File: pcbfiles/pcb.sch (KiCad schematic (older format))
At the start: 236 parts, among them J1 Conn_01x04_Female, J10 Conn_01x05, J2 Conn_01x05, J3 Conn_01x05, J4 Conn_01x05, J5 Conn_01x05, J6 Conn_01x04_Female, J7 Conn_01x05, J8 Conn_01x05, J9 Conn_01x05, Q1 AO3401A, Q2 AO3401A, SW1 SW_SPST, SW10 SW_SPST, SW11 SW_SPST, SW12 SW_SPST, SW13 SW_SPST, SW14 SW_SPST, SW15 SW_SPST, SW16 SW_SPST, SW17 SW_SPST, SW18 SW_SPST, SW19 SW_SPST, SW2 SW_SPST, SW20 SW_SPST, SW21 SW_SPST, SW22 SW_SPST, SW23 SW_SPST, SW24 SW_SPST, SW25 SW_SPST, SW26 SW_SPST, SW27 SW_SPST, SW28 SW_SPST, SW29 SW_SPST, SW3 SW_SPST, SW30 SW_SPST, SW31 SW_SPST, SW32 SW_SPST, SW33 SW_SPST, SW34 SW_SPST, SW35 SW_SPST, SW36 SW_SPST, SW37 SW_SPST, SW38 SW_SPDT, SW39 SW_SPST, SW4 SW_SPST, SW40 SW_SPST, SW41 SW_SPST, SW42 SW_SPST, SW43 SW_SPST, SW44 SW_SPST, SW45 SW_SPST, SW46 Rotary_Encoder_Switch, SW47 SW_SPDT, SW48 SW_SPST, SW49 SW_SPST, SW5 SW_SPST, SW50 SW_SPST, SW51 SW_SPST, SW52 SW_SPST, SW53 SW_SPST, SW54 SW_SPST, SW55 SW_SPST, SW56 SW_SPST, SW57 SW_SPST, SW58 SW_SPST, SW59 SW_SPST, SW6 SW_SPST, SW60 SW_SPST, SW61 SW_SPST, SW62 SW_SPST, SW63 SW_SPST, SW64 SW_SPST, SW65 SW_SPST, SW66 SW_SPST, SW67 SW_SPST, SW68 SW_SPST, SW69 SW_SPST, SW7 SW_SPST, SW70 SW_SPST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

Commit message: Final commit for the day.
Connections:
- net DB2_ROW_B is gone; now on net DB2_ROW0_B: J9.4 (Pin_4)
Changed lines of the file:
@@
 DB2_COL2_B
 Text GLabel 25750 6700 3    50   Input ~ 0
-DB2_ROW_B
+DB2_ROW0_B
 $Comp
 L power:GND1 #PWR0133

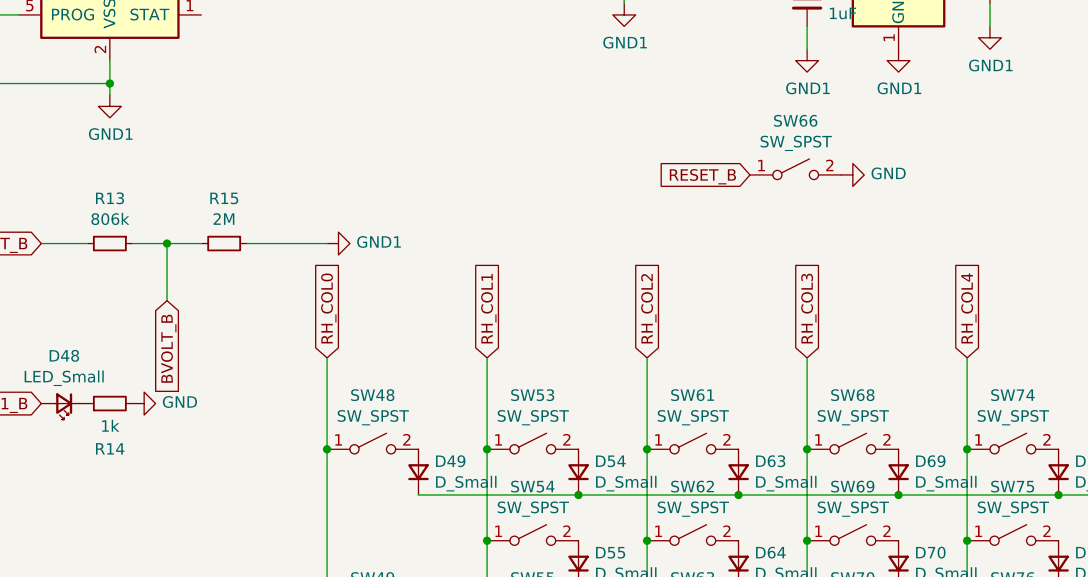
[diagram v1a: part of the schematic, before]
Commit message: Step file, various kinds of progress.
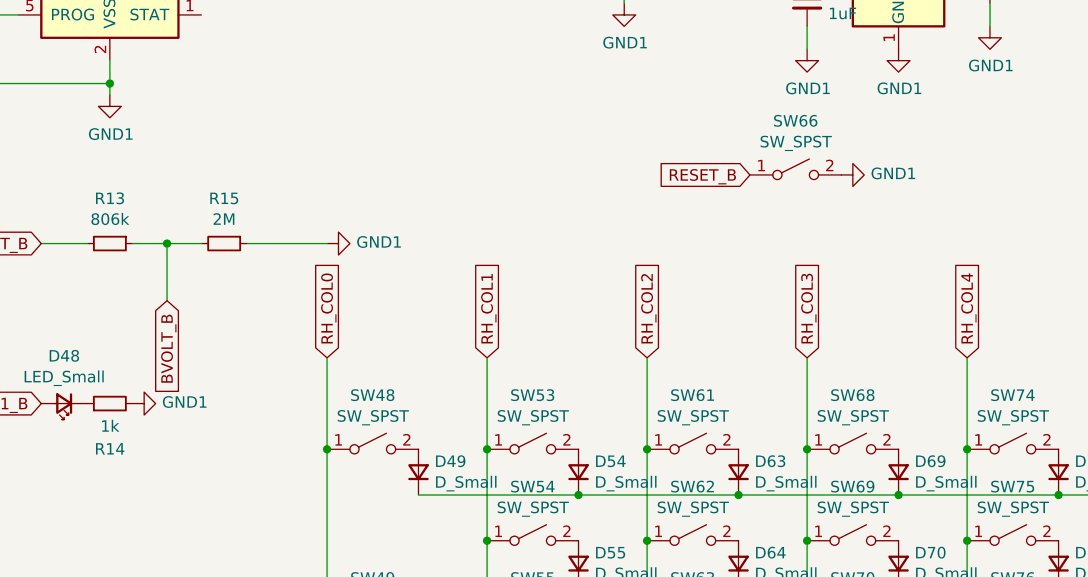
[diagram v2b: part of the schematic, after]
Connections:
- net GND: no longer R14.2, SW66.2 (B)
- net GND1: now also R14.2, SW66.2 (B)
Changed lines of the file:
@@
 $EndComp
 $Comp
-L power:GND #PWR0117
+L power:GND1 #PWR0117
 U 1 1 6132A644
 P 23450 2500
 F 0 "#PWR0117" H 23450 2250 50  0001 C CNN
-F 1 "GND" V 23455 2372 50  0000 R CNN
+F 1 "GND1" V 23455 2372 50  0000 R CNN
 F 2 "" H 23450 2500 50  0001 C CNN
 F 3 "" H 23450 2500 50  0001 C CNN
@@
 $EndComp
 $Comp
-L power:GND #PWR0118
+L power:GND1 #PWR0118
 U 1 1 6132A659
 P 20350 3500
 F 0 "#PWR0118" H 20350 3250 50  0001 C CNN
-F 1 "GND" V 20355 3372 50  0000 R CNN
+F 1 "GND1" V 20355 3372 50  0000 R CNN
 F 2 "" H 20350 3500 50  0001 C CNN
 F 3 "" H 20350 3500 50  0001 C CNN

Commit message: Routing progress.
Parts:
- BT1, BT3: footprint custom-parts:JST_PH_S2B-PH-K_1x02_P2.00mm_Horizontal -> Connector_JST:JST_PH_S2B-PH-K_1x02_P2.00mm_Horizontal
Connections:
- net DB1_COL0: now also U4.8 (P0.28)
- net DB1_COL1: now also U4.7 (P0.02)
- net DB1_ROW0: now also U4.6 (P0.03)
- net DB1_ROW1: now also U4.4 (P1.13)
- net LH_COL0: now also U4.2 (P1.11)
- net LH_COL1: now also U4.3 (P1.10)
- net LH_COL2: now also U4.10 (P0.30)
- net LH_ROW3: now also U4.9 (P0.29)
- net LH_ROW4: now also U4.11 (P0.31)
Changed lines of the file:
@@
 F 0 "BT1" V 4845 2100 50  0000 C CNN
 F 1 "Battery_Cell" V 4936 2100 50  0000 C CNN
-F 2 "custom-parts:JST_PH_S2B-PH-K_1x02_P2.00mm_Horizontal" V 5100 2110 50  0001 C CNN
+F 2 "Connector_JST:JST_PH_S2B-PH-K_1x02_P2.00mm_Horizontal" V 5100 2110 50  0001 C CNN
 F 3 "~" V 5100 2110 50  0001 C CNN
 	1    5100 2050
@@
 F 0 "BT3" V 19195 7050 50  0000 C CNN
 F 1 "Battery_Cell" V 19286 7050 50  0000 C CNN
-F 2 "custom-parts:JST_PH_S2B-PH-K_1x02_P2.00mm_Horizontal" V 19450 7060 50  0001 C CNN
+F 2 "Connector_JST:JST_PH_S2B-PH-K_1x02_P2.00mm_Horizontal" V 19450 7060 50  0001 C CNN
 F 3 "~" V 19450 7060 50  0001 C CNN
 	1    19450 7000
@@
 	21200 4900 21200 5700
 Connection ~ 21200 3700
+Text GLabel 900  4700 0    50   Input ~ 0
+LH_COL0
+Text GLabel 900  4800 0    50   Input ~ 0
+LH_COL1
+Text GLabel 900  5500 0    50   Input ~ 0
+LH_COL2
+Text GLabel 900  5300 0    50   Input ~ 0
+DB1_COL0
+Text GLabel 900  5200 0    50   Input ~ 0
+DB1_COL1
+Text GLabel 900  5100 0    50   Input ~ 0
+DB1_ROW0
+Text GLabel 900  4900 0    50   Input ~ 0
+DB1_ROW1
+Text GLabel 900  5400 0    50   Input ~ 0
+LH_ROW3
+Text GLabel 900  5600 0    50   Input ~ 0
+LH_ROW4
 $EndSCHEMATC

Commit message: more routing
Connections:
- net DB2_COL0_B: now also U1.11 (P0.31)
- net DB2_COL1_B: now also U1.10 (P0.30)
- net DB2_COL2_B: now also U1.9 (P0.29)
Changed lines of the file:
@@
 Text GLabel 900  5600 0    50   Input ~ 0
 LH_ROW4
+Text GLabel 16900 5600 0    50   Input ~ 0
+DB2_COL0_B
+Text GLabel 16900 5500 0    50   Input ~ 0
+DB2_COL1_B
+Text GLabel 16900 5400 0    50   Input ~ 0
+DB2_COL2_B
 $EndSCHEMATC

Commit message: Save most recent routing.
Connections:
- net DB1_COL0_B: now also U1.26 (P0.22)
- net DB1_COL1_B: now also U1.27 (P1.00)
- net DB1_ROW0_B: now also U1.28 (P1.03)
- net DB1_ROW1_B: now also U1.29 (P1.01)
- net DB2_ROW0_B: now also U1.8 (P0.28)
- net ENC_A_B: now also U1.2 (P1.11)
- net ENC_B_B: now also U1.3 (P1.10)
- net ENC_P1_B: now also U1.4 (P1.13)
- net RH_COL1: now also U1.18 (P0.23)
- net RH_COL2: now also U1.17 (P0.12)
- net RH_COL3: now also U1.16 (P1.09), U1.7 (P0.02)
- net RH_COL4: now also U1.15 (P0.07)
- net RH_COL5: now also U1.35 (P0.09)
- net RH_COL6: now also U1.36 (P0.10)
- net RH_ROW0: now also U1.33 (P1.04)
- net RH_ROW1: now also U1.34 (P1.06)
- net RH_ROW2: now also U1.30 (P1.02)
- net RH_ROW3: now also U1.20 (P0.19)
- net RH_ROW4: now also U1.13 (P0.05)
- net RH_ROW5: now also U1.6 (P0.03)
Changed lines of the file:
@@
 Text GLabel 16900 5400 0    50   Input ~ 0
 DB2_COL2_B
+Text GLabel 16900 5300 0    50   Input ~ 0
+DB2_ROW0_B
+Text GLabel 16900 5200 0    50   Input ~ 0
+RH_COL3
+Text GLabel 16900 5100 0    50   Input ~ 0
+RH_ROW5
+Text GLabel 16900 5800 0    50   Input ~ 0
+RH_ROW4
+Text GLabel 17500 6300 3    50   Input ~ 0
+RH_COL1
+Text GLabel 17200 6300 3    50   Input ~ 0
+RH_COL4
+Text GLabel 17300 6300 3    50   Input ~ 0
+RH_COL3
+Text GLabel 17400 6300 3    50   Input ~ 0
+RH_COL2
+Text GLabel 18300 5700 2    50   Input ~ 0
+DB1_COL0_B
+Text GLabel 18300 5600 2    50   Input ~ 0
+DB1_COL1_B
+Text GLabel 18300 5500 2    50   Input ~ 0
+DB1_ROW0_B
+Text GLabel 18300 5400 2    50   Input ~ 0
+DB1_ROW1_B
+Text GLabel 18300 4700 2    50   Input ~ 0
+RH_COL6
+Text GLabel 18300 4800 2    50   Input ~ 0
+RH_COL5
+Text GLabel 17700 6300 3    50   Input ~ 0
+RH_ROW3
+Text GLabel 18300 5300 2    50   Input ~ 0
+RH_ROW2
+Text GLabel 18300 4900 2    50   Input ~ 0
+RH_ROW1
+Text GLabel 18300 5000 2    50   Input ~ 0
+RH_ROW0
+Text GLabel 16900 4900 0    50   Input ~ 0
+RH_COL0
+Text GLabel 16900 4800 0    30   Input ~ 0
+ENC_B_B
+Text GLabel 16900 4700 0    30   Input ~ 0
+ENC_A_B
 $EndSCHEMATC

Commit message: Finish all basic routing!
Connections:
- net DB2_COL0: now also U4.19 (P0.21)
- net DB2_COL1: now also U4.18 (P0.23)
- net DB2_COL2: now also U4.17 (P0.12)
- net DB2_ROW0: now also U4.16 (P1.09)
- net ENC_A: now also U4.33 (P1.04)
- net ENC_B: now also U4.30 (P1.02)
- net ENC_P1: now also U4.34 (P1.06)
- net LH_COL3: now also U4.20 (P0.19)
- net LH_COL4: now also U4.26 (P0.22)
- net LH_COL5: now also U4.35 (P0.09)
- net LH_ROW0: now also U4.27 (P1.00)
- net LH_ROW1: now also U4.28 (P1.03)
- net LH_ROW2: now also U4.29 (P1.01)
- net LH_ROW5: now also U4.36 (P0.10)
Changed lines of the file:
@@
 Text GLabel 16900 4700 0    30   Input ~ 0
 ENC_A_B
+Text GLabel 1700 6300 3    50   Input ~ 0
+LH_COL3
+Text GLabel 2300 4800 2    50   Input ~ 0
+LH_COL5
+Text GLabel 1600 6300 3    50   Input ~ 0
+DB2_COL0
+Text GLabel 1500 6300 3    50   Input ~ 0
+DB2_COL1
+Text GLabel 1400 6300 3    50   Input ~ 0
+DB2_COL2
+Text GLabel 1300 6300 3    50   Input ~ 0
+DB2_ROW0
+Text GLabel 2300 4900 2    50   Input ~ 0
+LH_COL6
+Text GLabel 2300 4700 2    50   Input ~ 0
+LH_ROW5
+Text GLabel 2300 5700 2    50   Input ~ 0
+LH_COL4
+Text GLabel 2300 5000 2    30   Input ~ 0
+ENC_A
+Text GLabel 2300 5300 2    30   Input ~ 0
+ENC_B
+Text GLabel 2300 5400 2    50   Input ~ 0
+LH_ROW2
+Text GLabel 2300 5600 2    50   Input ~ 0
+LH_ROW0
+Text GLabel 2300 5500 2    50   Input ~ 0
+LH_ROW1
 $EndSCHEMATC

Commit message: Almost there!
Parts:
- BT2, BT4: footprint custom-parts:custombatteryconnector -> kicad-keyboard-parts:battery-custom-connector
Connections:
- net DB1_COL0: now also J2.2 (Pin_2), J3.2 (Pin_2); no longer J2.1 (Pin_1), J3.1 (Pin_1)
- net DB1_COL0_B: now also J7.2 (Pin_2), J8.2 (Pin_2); no longer J7.1 (Pin_1), J8.1 (Pin_1)
- net DB1_COL1: now also J2.4 (Pin_4), J3.4 (Pin_4); no longer J2.2 (Pin_2), J3.2 (Pin_2)
- net DB1_COL1_B: now also J7.4 (Pin_4), J8.4 (Pin_4); no longer J7.2 (Pin_2), J8.2 (Pin_2)
- net DB1_ROW0: now also J2.1 (Pin_1), J3.1 (Pin_1); no longer J2.3 (Pin_3), J3.3 (Pin_3)
- net DB1_ROW0_B: now also J7.1 (Pin_1), J8.1 (Pin_1); no longer J7.3 (Pin_3), J8.3 (Pin_3)
- net DB1_ROW1: now also J2.3 (Pin_3), J3.3 (Pin_3); no longer J2.4 (Pin_4), J3.4 (Pin_4)
- net DB1_ROW1_B: now also J7.3 (Pin_3), J8.3 (Pin_3); no longer J7.4 (Pin_4), J8.4 (Pin_4)
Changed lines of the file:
@@
 F 0 "BT2" V 4845 2500 50  0000 C CNN
 F 1 "Battery_Cell" V 4936 2500 50  0000 C CNN
-F 2 "custom-parts:custombatteryconnector" V 5100 2510 50  0001 C CNN
+F 2 "kicad-keyboard-parts:battery-custom-connector" V 5100 2510 50  0001 C CNN
 F 3 "~" V 5100 2510 50  0001 C CNN
 	1    5100 2450
@@
 F 0 "BT4" V 19195 7450 50  0000 C CNN
 F 1 "Battery_Cell" V 19286 7450 50  0000 C CNN
-F 2 "custom-parts:custombatteryconnector" V 19450 7460 50  0001 C CNN
+F 2 "kicad-keyboard-parts:battery-custom-connector" V 19450 7460 50  0001 C CNN
 F 3 "~" V 19450 7460 50  0001 C CNN
 	1    19450 7400
@@
 	0    -1   -1   0
 $EndComp
-Text GLabel 6050 7250 3    50   Input ~ 0
-DB1_COL0
 Text GLabel 6150 7250 3    50   Input ~ 0
+DB1_COL0
+Text GLabel 6350 7250 3    50   Input ~ 0
 DB1_COL1
-Text GLabel 6250 7250 3    50   Input ~ 0
+Text GLabel 6050 7250 3    50   Input ~ 0
 DB1_ROW0
-Text GLabel 6350 7250 3    50   Input ~ 0
+Text GLabel 6250 7250 3    50   Input ~ 0
 DB1_ROW1
 Wire Wire Line
@@
 	0    -1   -1   0
 $EndComp
-Text GLabel 6750 7250 3    50   Input ~ 0
-DB1_COL0
-Text GLabel 6850 7250 3    50   Input ~ 0
-DB1_COL1
-Text GLabel 6950 7250 3    50   Input ~ 0
-DB1_ROW0
-Text GLabel 7050 7250 3    50   Input ~ 0
-DB1_ROW1
 $Comp
 L power:GND #PWR0126
@@
 	0    -1   -1   0
 $EndComp
-Text GLabel 22250 6700 3    50   Input ~ 0
-DB1_COL0_B
 Text GLabel 22350 6700 3    50   Input ~ 0
+DB1_COL0_B
+Text GLabel 22550 6700 3    50   Input ~ 0
 DB1_COL1_B
-Text GLabel 22450 6700 3    50   Input ~ 0
+Text GLabel 22250 6700 3    50   Input ~ 0
 DB1_ROW0_B
-Text GLabel 22550 6700 3    50   Input ~ 0
+Text GLabel 22450 6700 3    50   Input ~ 0
 DB1_ROW1_B
 Wire Wire Line
@@
 	0    -1   -1   0
 $EndComp
-Text GLabel 22950 6700 3    50   Input ~ 0
-DB1_COL0_B
-Text GLabel 23050 6700 3    50   Input ~ 0
-DB1_COL1_B
-Text GLabel 23150 6700 3    50   Input ~ 0
-DB1_ROW0_B
-Text GLabel 23250 6700 3    50   Input ~ 0
-DB1_ROW1_B
 $Comp
 L power:GND1 #PWR0131
@@
 $EndComp
 $Comp
-L power:GND1 #PWR0132
-U 1 1 6175E9C4
-P 23350 6700
-F 0 "#PWR0132" H 23350 6450 50  0001 C CNN
-F 1 "GND1" H 23355 6527 50  0000 C CNN
-F 2 "" H 23350 6700 50  0001 C CNN
-F 3 "" H 23350 6700 50  0001 C CNN
-	1    23350 6700
-	1    0    0    -1
-$EndComp
-$Comp
 L Connector_Generic:Conn_01x05 J9
 U 1 1 6175E9CA
@@
 Text GLabel 2300 5500 2    50   Input ~ 0
 LH_ROW1
+Text GLabel 6850 7250 3    50   Input ~ 0
+DB1_COL0
+Text GLabel 7050 7250 3    50   Input ~ 0
+DB1_COL1
+Text GLabel 6750 7250 3    50   Input ~ 0
+DB1_ROW0
+Text GLabel 6950 7250 3    50   Input ~ 0
+DB1_ROW1
+Text GLabel 23050 6700 3    50   Input ~ 0
+DB1_COL0_B
+Text GLabel 23250 6700 3    50   Input ~ 0
+DB1_COL1_B
+Text GLabel 22950 6700 3    50   Input ~ 0
+DB1_ROW0_B
+Text GLabel 23150 6700 3    50   Input ~ 0
+DB1_ROW1_B
+$Comp
+L power:GND1 #PWR0132
+U 1 1 61585969
+P 23350 6700
+F 0 "#PWR0132" H 23350 6450 50  0001 C CNN
+F 1 "GND1" H 23355 6527 50  0000 C CNN
+F 2 "" H 23350 6700 50  0001 C CNN
+F 3 "" H 23350 6700 50  0001 C CNN
+	1    23350 6700
+	1    0    0    -1
+$EndComp
 $EndSCHEMATC

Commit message: finished commit sans production files
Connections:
- net DB1_COL0: now also U4.7 (P0.02); no longer U4.8 (P0.28)
- net DB1_COL0_B: now also U1.27 (P1.00); no longer U1.26 (P0.22)
- net DB1_COL1: now also U4.4 (P1.13); no longer U4.7 (P0.02)
- net DB1_COL1_B: now also U1.29 (P1.01); no longer U1.27 (P1.00)
- net DB1_ROW0: now also U4.8 (P0.28); no longer U4.6 (P0.03)
- net DB1_ROW0_B: now also U1.26 (P0.22); no longer U1.28 (P1.03)
- net DB1_ROW1: now also U4.6 (P0.03); no longer U4.4 (P1.13)
- net DB1_ROW1_B: now also U1.28 (P1.03); no longer U1.29 (P1.01)
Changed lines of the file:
@@
 Text GLabel 900  5500 0    50   Input ~ 0
 LH_COL2
+Text GLabel 900  5200 0    50   Input ~ 0
+DB1_COL0
+Text GLabel 900  4900 0    50   Input ~ 0
+DB1_COL1
 Text GLabel 900  5300 0    50   Input ~ 0
-DB1_COL0
-Text GLabel 900  5200 0    50   Input ~ 0
-DB1_COL1
+DB1_ROW0
 Text GLabel 900  5100 0    50   Input ~ 0
-DB1_ROW0
-Text GLabel 900  4900 0    50   Input ~ 0
 DB1_ROW1
 Text GLabel 900  5400 0    50   Input ~ 0
@@
 Text GLabel 16900 5500 0    50   Input ~ 0
 DB2_COL1_B
-Text GLabel 16900 5400 0    50   Input ~ 0
-DB2_COL2_B
-Text GLabel 16900 5300 0    50   Input ~ 0
-DB2_ROW0_B
 Text GLabel 16900 5200 0    50   Input ~ 0
 RH_COL3
@@
 Text GLabel 17400 6300 3    50   Input ~ 0
 RH_COL2
+Text GLabel 18300 5600 2    50   Input ~ 0
+DB1_COL0_B
+Text GLabel 18300 5400 2    50   Input ~ 0
+DB1_COL1_B
 Text GLabel 18300 5700 2    50   Input ~ 0
-DB1_COL0_B
-Text GLabel 18300 5600 2    50   Input ~ 0
-DB1_COL1_B
+DB1_ROW0_B
 Text GLabel 18300 5500 2    50   Input ~ 0
-DB1_ROW0_B
-Text GLabel 18300 5400 2    50   Input ~ 0
 DB1_ROW1_B
 Text GLabel 18300 4700 2    50   Input ~ 0
@@
 	1    0    0    -1
 $EndComp
+Text GLabel 16900 5300 0    50   Input ~ 0
+DB2_ROW0_B
+Text GLabel 16900 5400 0    50   Input ~ 0
+DB2_COL2_B
 $EndSCHEMATC
